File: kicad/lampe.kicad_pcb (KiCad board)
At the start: 2 copper layers, 67.9 x 66.7 mm, 86 parts, among them U1 WeMos_D1_mini, X1 SW_Push, Y1 SW_Push

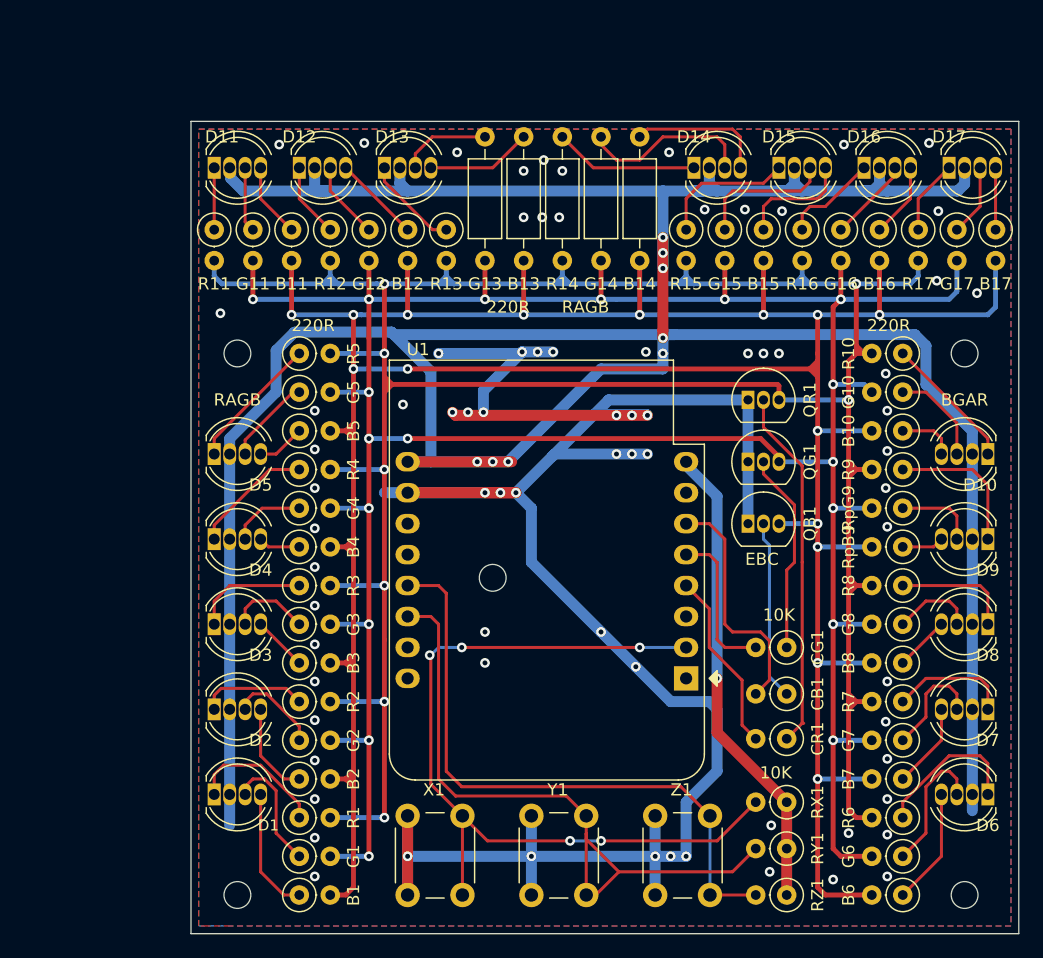
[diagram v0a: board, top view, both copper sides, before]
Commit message: +transistor and led footprint edit => spread the legs... euh
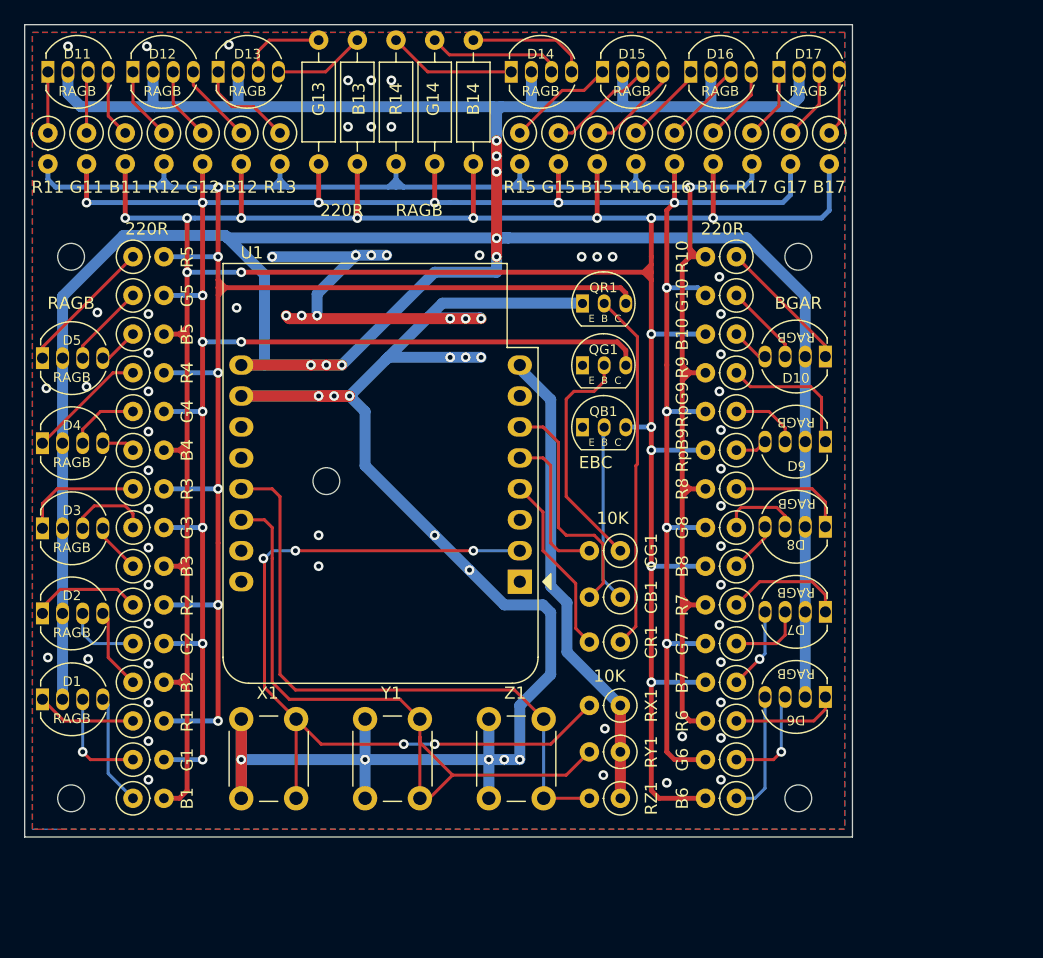
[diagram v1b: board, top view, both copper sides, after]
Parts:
- D1, D10, D11, D12, D13, D14, D15, D16, D17, D2, D3, D4, D5, D6, D7, D8, D9: footprint LED_THT:LED_D5.0mm-4_RGB -> pierre:LED_RAGB_5mm_v2
- QB1, QG1, QR1: footprint Package_TO_SOT_THT:TO-92_Inline -> pierre:Q_NPN_EBC_TO-92_v2
- moved D14 17.0 mm to (216.8, 100.0)
- moved D15 16.5 mm to (224.3, 100.0)
- moved D16 16.3 mm to (231.5, 100.0)
- moved D2 16.2 mm to (178.3, 144.5)
- moved D3 16.2 mm to (178.3, 137.5)
- moved D4 16.2 mm to (178.3, 130.5)
- moved D5 16.2 mm to (178.3, 123.5)
- moved D1 16.1 mm to (178.3, 151.5)
- moved D17 16.1 mm to (238.8, 100.0)
- moved B17 15.8 mm to (242.9, 105.1)
- moved QG1 15.8 mm to (222.6, 124.1)
- moved B11 15.8 mm to (185.1, 105.1)
- moved B12 15.8 mm to (194.6, 105.1)
- moved B13 15.8 mm to (204.2, 97.5)
- moved B14 15.8 mm to (213.7, 97.5)
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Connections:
- U1 pad 1: Net-(U1-Pad1) -> unconnected-(U1-Pad1)
- U1 pad 11: Net-(U1-Pad11) -> unconnected-(U1-Pad11)
- U1 pad 12: Net-(U1-Pad12) -> unconnected-(U1-Pad12)
- U1 pad 15: Net-(U1-Pad15) -> unconnected-(U1-Pad15)
- U1 pad 16: Net-(U1-Pad16) -> unconnected-(U1-Pad16)
- U1 pad 3: Net-(U1-Pad3) -> unconnected-(U1-Pad3)
- U1 pad 7: Net-(U1-Pad7) -> unconnected-(U1-Pad7)
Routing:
- net GND: track 187.0 -> 174.9 mm, vias 77 -> 75
- net +5V: track 283.5 -> 273.8 mm
- net /pR: track 246.0 -> 241.2 mm, vias 8 -> 7
- net Net-(D6-Pad1): track 12.6 -> 8.71 mm
- net Net-(D14-Pad3): track 14.3 -> 11.0 mm
- net Net-(D1-Pad1): track 11.4 -> 8.17 mm
- net /pG: track 242.1 -> 239.2 mm, vias 18 -> 17
- net Net-(CG1-Pad1): track 16.6 -> 19.3 mm
- net Net-(D7-Pad3): track 8.94 -> 6.20 mm
- net Net-(D6-Pad3): track 11.1 -> 8.59 mm, vias 0 -> 1
- net Net-(D15-Pad1): track 11.2 -> 8.87 mm
- net Net-(D15-Pad3): track 11.3 -> 9.00 mm
- net Net-(B10-Pad1): track 4.71 -> 3.11 mm
- net Net-(D2-Pad3): track 7.58 -> 6.12 mm
- net Net-(B15-Pad1): track 9.42 -> 7.96 mm
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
